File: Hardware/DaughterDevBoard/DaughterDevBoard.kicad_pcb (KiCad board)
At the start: 2 copper layers, 145 x 160 mm, 73 parts, among them J1 PS/2, J10 I/O_PWR, J11 DIVIDER, J12 AUDIO_OUT, J13 BANKA, J14 BANKB, J15 BANKD, J16 BANKC, J17 VGA_OUT, J18 SD_CARD, J19 BANK_A, J2 I/O0, J20 BANK_C, J21 BANK_B, J22 BANK_D, J3 ISA1, J4 ISA0, J5 I/O1, J6 CPU_CLOCK, J7 JOYPAD1, J8 PROG, J9 LCD, Q1 2N2222A, U1 74HC590A, U2 ATmega328P-PU, U3 SN74LVC2T45QDCURQ1, U4 SN74LVC2T45QDCURQ1, U5 NE555P, U6 SN74LVC8T245DBQR, U7 SN74LVC8T245DBQR, U8 SN74LVC8T245DBQR, U9 SN74LVC1T45DCK, X1 ACO-20MHz

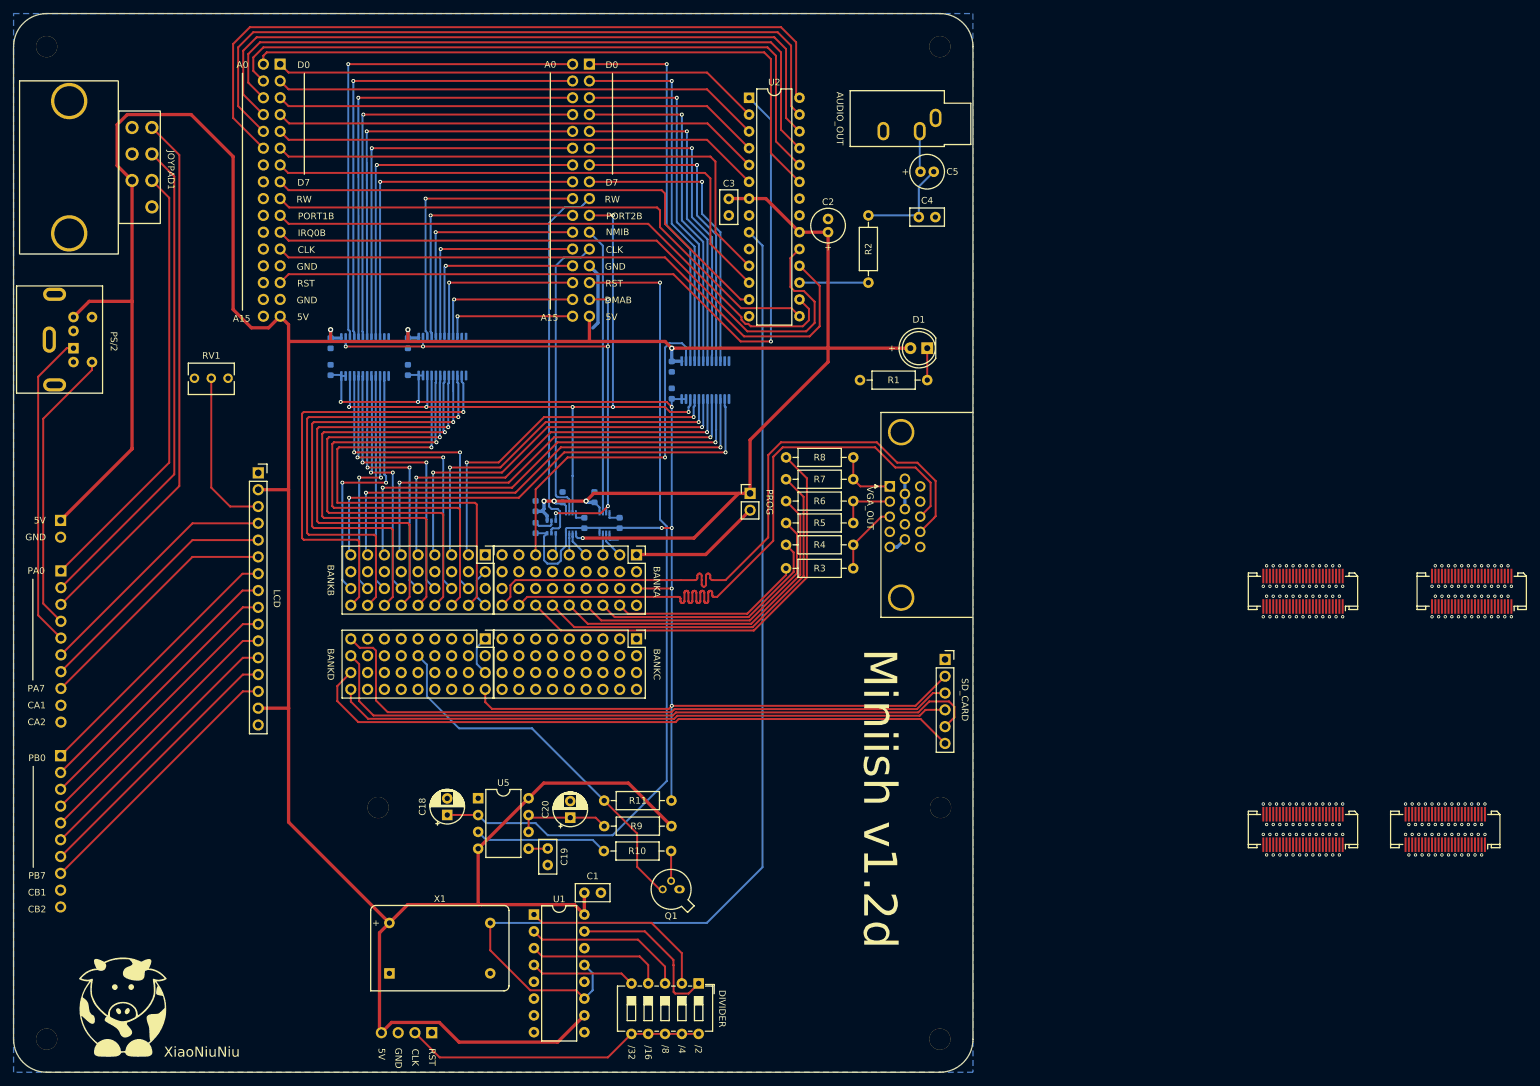
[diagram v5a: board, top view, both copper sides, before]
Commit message: Remove Alchitry shield
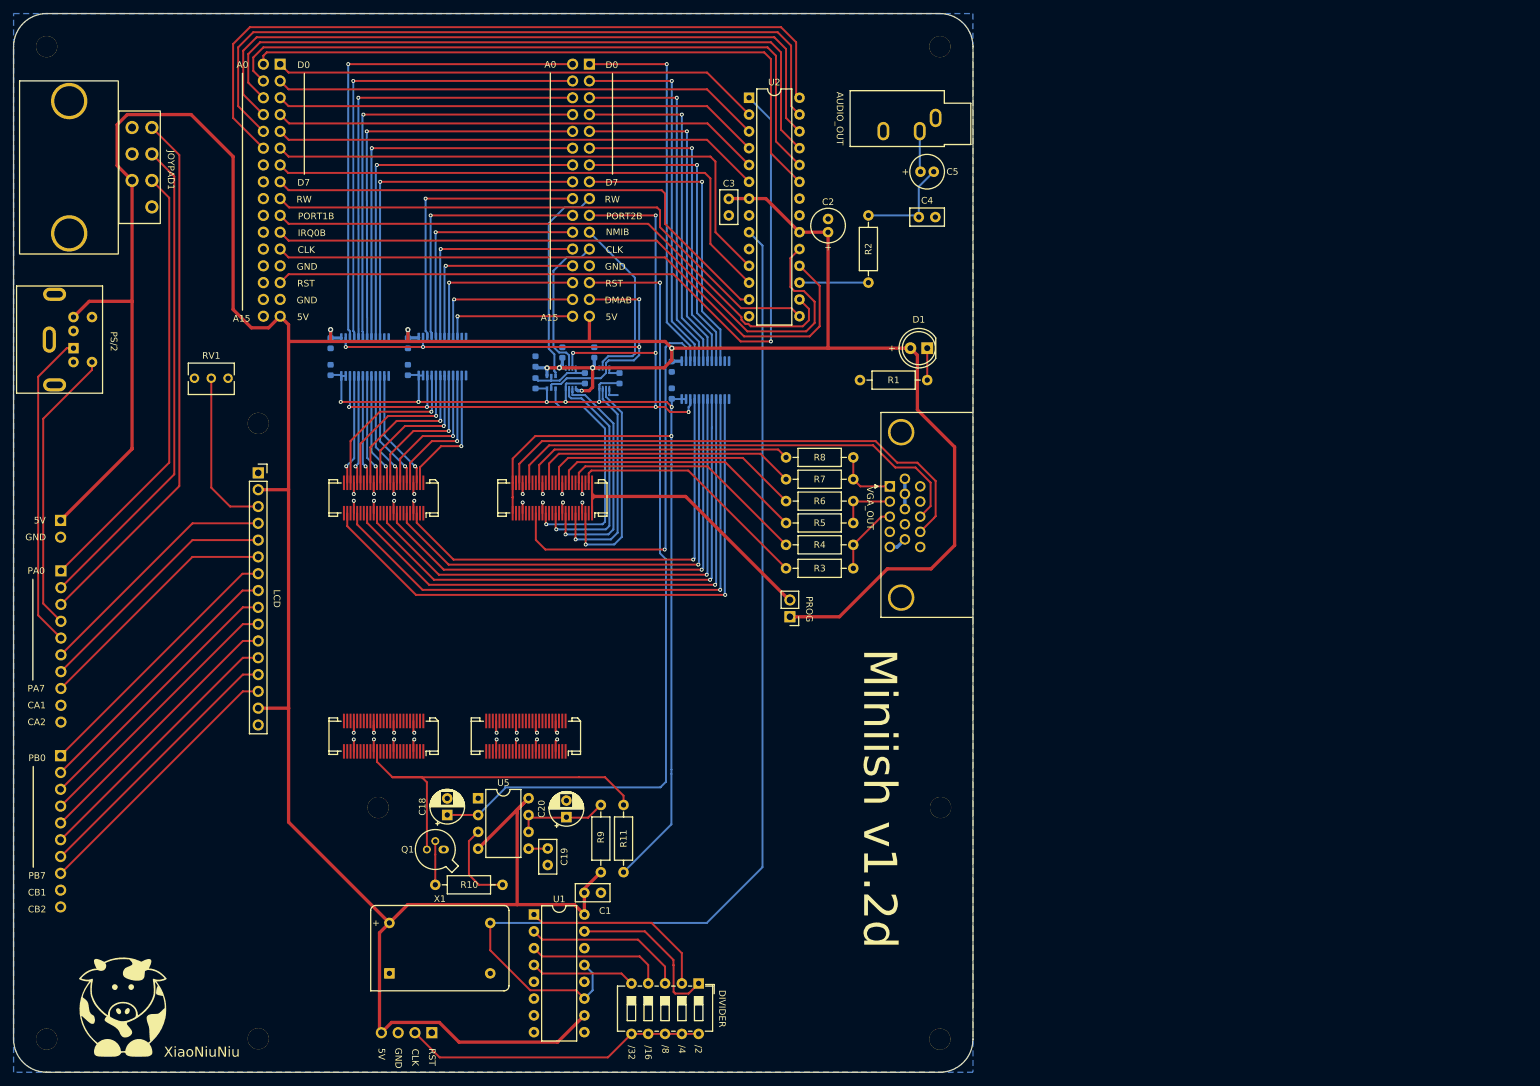
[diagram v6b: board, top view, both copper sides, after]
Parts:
- removed J13: BANKA, Connector_TheRLab:Alchitry_Bank
- removed J14: BANKB, Connector_TheRLab:Alchitry_Bank
- removed J15: BANKD, Connector_TheRLab:Alchitry_Bank
- removed J16: BANKC, Connector_TheRLab:Alchitry_Bank
- removed J18: SD_CARD, Connector_PinSocket_2.54mm:PinSocket_1x06_P2.54mm_Vertical
- added H7: MountingHole_Pad, , F.Cu at (62.5, 87.3)
- added H8: MountingHole_Pad, , F.Cu at (62.5, 180.3)
- R3, R5, R7: value 1.5K -> 1K
- R4, R6, R8: value 680 -> 470
- moved J19 139.7 mm to (106.9, 98.6)
- moved J20 139.7 mm to (81.4, 98.6)
- moved J21 139.7 mm to (102.9, 134.6)
- moved J22 139.7 mm to (81.4, 134.6)
- moved Q1 36.1 mm to (90.5, 151.7)
- moved C11 21.9 mm to (111.8, 80.5)
- moved C6 21.9 mm to (104.4, 78.0)
- moved C7 21.9 mm to (113.3, 76.6)
- moved C10 21.9 mm to (104.4, 81.3)
- moved C13 21.9 mm to (117.1, 80.5)
- moved C8 21.9 mm to (108.4, 76.6)
- moved U3 21.9 mm to (114.8, 80.5)
- moved U4 21.9 mm to (109.7, 80.5)
- moved U9 21.9 mm to (106.8, 81.1)
- moved J8 19.6 mm to (142.8, 116.5), turned to 180 degrees
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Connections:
- C12 pad 1: +5V -> GND
- C12 pad 2: GND -> +5V
- C14 pad 1: +5V -> GND
- C14 pad 2: GND -> +5V
- C16 pad 1: +5V -> GND
- C16 pad 2: GND -> +5V
- J19 pad 1: unconnected-(J19-Pad1) -> Net-(J19-Pad1)
- J19 pad 10: unconnected-(J19-Pad10) -> GND
- J19 pad 11: unconnected-(J19-Pad11) -> /VGA Card/DB3
- J19 pad 14: unconnected-(J19-Pad14) -> /VGA Card/DB4
- J19 pad 16: unconnected-(J19-Pad16) -> GND
- J19 pad 17: unconnected-(J19-Pad17) -> /VGA Card/DB5
- J19 pad 2: unconnected-(J19-Pad2) -> /VGA Card/DB0
- J19 pad 20: unconnected-(J19-Pad20) -> /VGA Card/HSYNC
- J19 pad 22: unconnected-(J19-Pad22) -> GND
- J19 pad 23: unconnected-(J19-Pad23) -> /VGA Card/VSYNC
- J19 pad 25: unconnected-(J19-Pad25) -> +3V3
- J19 pad 26: unconnected-(J19-Pad26) -> +3V3
- J19 pad 29: unconnected-(J19-Pad29) -> GND
- J19 pad 33: unconnected-(J19-Pad33) -> /VGA Card/DMARW
- J19 pad 35: unconnected-(J19-Pad35) -> GND
- J19 pad 36: unconnected-(J19-Pad36) -> /VGA Card/A36
- J19 pad 39: unconnected-(J19-Pad39) -> /VGA Card/A39
- J19 pad 4: unconnected-(J19-Pad4) -> GND
- J19 pad 41: unconnected-(J19-Pad41) -> GND
- J19 pad 42: unconnected-(J19-Pad42) -> /VGA Card/A42
- J19 pad 45: unconnected-(J19-Pad45) -> /VGA Card/A45
- J19 pad 47: unconnected-(J19-Pad47) -> GND
- J19 pad 48: unconnected-(J19-Pad48) -> /VGA Card/A48
- J19 pad 5: unconnected-(J19-Pad5) -> /VGA Card/DB1
- J19 pad 50: unconnected-(J19-Pad50) -> Net-(J19-Pad1)
- J19 pad 8: unconnected-(J19-Pad8) -> /VGA Card/DB2
- J20 pad 10: unconnected-(J20-Pad10) -> GND
- J20 pad 11: unconnected-(J20-Pad11) -> /VGA Card/B11
- J20 pad 12: unconnected-(J20-Pad12) -> /VGA Card/B12
- J20 pad 14: unconnected-(J20-Pad14) -> /VGA Card/B14
- J20 pad 15: unconnected-(J20-Pad15) -> /VGA Card/B15
- J20 pad 16: unconnected-(J20-Pad16) -> GND
- J20 pad 17: unconnected-(J20-Pad17) -> /VGA Card/B17
- J20 pad 18: unconnected-(J20-Pad18) -> /VGA Card/B18
- J20 pad 2: unconnected-(J20-Pad2) -> /VGA Card/B02
- J20 pad 20: unconnected-(J20-Pad20) -> /VGA Card/B20
- J20 pad 21: unconnected-(J20-Pad21) -> /VGA Card/B21
- J20 pad 22: unconnected-(J20-Pad22) -> GND
- J20 pad 23: unconnected-(J20-Pad23) -> /VGA Card/B23
- J20 pad 24: unconnected-(J20-Pad24) -> /VGA Card/B24
- J20 pad 27: unconnected-(J20-Pad27) -> /VGA Card/B27
- J20 pad 29: unconnected-(J20-Pad29) -> GND
- J20 pad 3: unconnected-(J20-Pad3) -> /VGA Card/B03
- J20 pad 30: unconnected-(J20-Pad30) -> /VGA Card/B30
- J20 pad 33: unconnected-(J20-Pad33) -> /VGA Card/B33
- J20 pad 35: unconnected-(J20-Pad35) -> GND
- J20 pad 36: unconnected-(J20-Pad36) -> /VGA Card/B36
- J20 pad 39: unconnected-(J20-Pad39) -> /VGA Card/B39
- J20 pad 4: unconnected-(J20-Pad4) -> GND
- J20 pad 41: unconnected-(J20-Pad41) -> GND
- J20 pad 42: unconnected-(J20-Pad42) -> /VGA Card/B42
- J20 pad 45: unconnected-(J20-Pad45) -> /VGA Card/B45
- J20 pad 47: unconnected-(J20-Pad47) -> GND
- J20 pad 48: unconnected-(J20-Pad48) -> /VGA Card/B48
- J20 pad 5: unconnected-(J20-Pad5) -> /VGA Card/B05
- J20 pad 6: unconnected-(J20-Pad6) -> /VGA Card/B06
- J20 pad 8: unconnected-(J20-Pad8) -> /VGA Card/B08
- J20 pad 9: unconnected-(J20-Pad9) -> /VGA Card/B09
- J21 pad 10: unconnected-(J21-Pad10) -> GND
- J21 pad 16: unconnected-(J21-Pad16) -> GND
- J21 pad 22: unconnected-(J21-Pad22) -> GND
- J21 pad 29: unconnected-(J21-Pad29) -> GND
- J21 pad 35: unconnected-(J21-Pad35) -> GND
- J21 pad 4: unconnected-(J21-Pad4) -> GND
- J21 pad 41: unconnected-(J21-Pad41) -> GND
- J21 pad 47: unconnected-(J21-Pad47) -> GND
- J22 pad 10: unconnected-(J22-Pad10) -> GND
- J22 pad 16: unconnected-(J22-Pad16) -> GND
- J22 pad 22: unconnected-(J22-Pad22) -> GND
- J22 pad 29: unconnected-(J22-Pad29) -> GND
- J22 pad 35: unconnected-(J22-Pad35) -> GND
- J22 pad 36: unconnected-(J22-Pad36) -> /VGA Card/D36
- J22 pad 4: unconnected-(J22-Pad4) -> GND
- J22 pad 41: unconnected-(J22-Pad41) -> GND
- J22 pad 47: unconnected-(J22-Pad47) -> GND
- J8 pad 2: Net-(J13-Pad1) -> Net-(J19-Pad1)
- Q1 pad 3: Net-(J15-Pad14) -> /VGA Card/D36
- R11 pad 1: Net-(J15-Pad14) -> /VGA Card/D36
- U3 pad 6: Net-(J13-Pad2) -> /VGA Card/A48
- U3 pad 7: Net-(J13-Pad3) -> /VGA Card/A45
- U4 pad 6: Net-(J13-Pad4) -> /VGA Card/A42
- U4 pad 7: Net-(J13-Pad5) -> /VGA Card/A39
- U6 pad 14: Net-(J14-Pad9) -> /VGA Card/B27
- U6 pad 15: Net-(J14-Pad8) -> /VGA Card/B30
- U6 pad 16: Net-(J14-Pad7) -> /VGA Card/B33
- U6 pad 17: Net-(J14-Pad6) -> /VGA Card/B36
- U6 pad 18: Net-(J14-Pad5) -> /VGA Card/B39
- U6 pad 19: Net-(J14-Pad4) -> /VGA Card/B42
- U6 pad 20: Net-(J14-Pad3) -> /VGA Card/B45
- U6 pad 21: Net-(J14-Pad2) -> /VGA Card/B48
- U7 pad 14: Net-(J14-Pad28) -> /VGA Card/B02
- U7 pad 15: Net-(J14-Pad29) -> /VGA Card/B05
- U7 pad 16: Net-(J14-Pad30) -> /VGA Card/B08
- U7 pad 17: Net-(J14-Pad31) -> /VGA Card/B11
- U7 pad 18: Net-(J14-Pad32) -> /VGA Card/B14
- U7 pad 19: Net-(J14-Pad33) -> /VGA Card/B17
- U7 pad 20: Net-(J14-Pad34) -> /VGA Card/B20
- U7 pad 21: Net-(J14-Pad35) -> /VGA Card/B23
- U8 pad 14: Net-(J14-Pad19) -> /VGA Card/B03
- U8 pad 15: Net-(J14-Pad20) -> /VGA Card/B06
- U8 pad 16: Net-(J14-Pad21) -> /VGA Card/B09
- U8 pad 17: Net-(J14-Pad22) -> /VGA Card/B12
- U8 pad 18: Net-(J14-Pad23) -> /VGA Card/B15
- U8 pad 19: Net-(J14-Pad24) -> /VGA Card/B18
- U8 pad 20: Net-(J14-Pad25) -> /VGA Card/B21
- U8 pad 21: Net-(J14-Pad26) -> /VGA Card/B24
- U9 pad 3: /VGA Card/DMAB -> /VGA Card/RW
- U9 pad 4: Net-(J13-Pad6) -> /VGA Card/A36
- U9 pad 5: /VGA Card/RW -> /VGA Card/DMAB
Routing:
- net SCK: track 103.1 -> 0.00 mm
- net MISO: track 100.0 -> 0.00 mm
- net SS: track 100.0 -> 0.00 mm
- net MOSI: track 93.3 -> 0.00 mm
- net /VGA Card/B27: track 0.00 -> 93.0 mm, vias 0 -> 1
- net /VGA Card/B30: track 0.00 -> 89.5 mm, vias 0 -> 1
- net /VGA Card/B33: track 0.00 -> 86.1 mm, vias 0 -> 1
- net /VGA Card/B36: track 0.00 -> 82.8 mm, vias 0 -> 1
- net /VGA Card/B39: track 0.00 -> 79.6 mm, vias 0 -> 1
- net /VGA Card/B42: track 0.00 -> 76.3 mm, vias 0 -> 1
- net Net-(J14-Pad9): track 76.2 -> 0.00 mm, vias 3 -> 0
- net /VGA Card/B45: track 0.00 -> 73.2 mm, vias 0 -> 1
- net Net-(J14-Pad8): track 72.9 -> 0.00 mm, vias 3 -> 0
- net Net-(J14-Pad35): track 70.3 -> 0.00 mm, vias 1 -> 0
- net Net-(J14-Pad34): track 69.9 -> 0.00 mm, vias 1 -> 0
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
